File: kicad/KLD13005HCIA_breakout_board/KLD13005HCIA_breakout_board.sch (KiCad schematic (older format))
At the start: 7 parts, among them J1 Pin Headers, J2 Conn_01x24_Male, J3 Capacitive Touch Sensor, Q1 Q_NMOS_GSD

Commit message: Create initial PCB design
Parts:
- J1: footprint (none) -> Connector_PinSocket_2.54mm:PinSocket_1x10_P2.54mm_Vertical
- J2: footprint (none) -> 687124183622:687124183622
- J3: footprint (none) -> BM20B(0.8)-10DS-0.4V(51):BM20B(0.8)-10DS-0.4V(51)
- Q1: footprint (none) -> bss138:BSS138
- R1, R2, R3: footprint (none) -> Resistor_SMD:R_0603_1608Metric
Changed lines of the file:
@@
 F 0 "J1" H 950 2150 50  0000 C CNN
 F 1 "Pin Headers" H 1000 2050 50  0000 C CNN
-F 2 "" H 850 1450 50  0001 C CNN
+F 2 "Connector_PinSocket_2.54mm:PinSocket_1x10_P2.54mm_Vertical" H 850 1450 50  0001 C CNN
 F 3 "~" H 850 1450 50  0001 C CNN
 	1    850  1450
@@
 F 0 "J3" H 4250 1767 50  0000 C CNN
 F 1 "Capacitive Touch Sensor" H 4250 1676 50  0000 C CNN
-F 2 "" H 4200 1350 50  0001 C CNN
+F 2 "BM20B(0.8)-10DS-0.4V(51):BM20B(0.8)-10DS-0.4V(51)" H 4200 1350 50  0001 C CNN
 F 3 "~" H 4200 1350 50  0001 C CNN
 	1    4200 1350
@@
 F 0 "R2" H 4209 2246 50  0000 L CNN
 F 1 "10K" H 4209 2155 50  0000 L CNN
-F 2 "" H 4150 2200 50  0001 C CNN
+F 2 "Resistor_SMD:R_0603_1608Metric" H 4150 2200 50  0001 C CNN
 F 3 "~" H 4150 2200 50  0001 C CNN
 	1    4150 2200
@@
 F 0 "Q1" H 4105 3296 50  0000 L CNN
 F 1 "Q_NMOS_GSD" H 4105 3205 50  0000 L CNN
-F 2 "" H 4100 3350 50  0001 C CNN
+F 2 "bss138:BSS138" H 4100 3350 50  0001 C CNN
 F 3 "~" H 3900 3250 50  0001 C CNN
 	1    3900 3250
@@
 F 0 "R1" H 3859 2896 50  0000 L CNN
 F 1 "10K" H 3859 2805 50  0000 L CNN
-F 2 "" H 3800 2850 50  0001 C CNN
+F 2 "Resistor_SMD:R_0603_1608Metric" H 3800 2850 50  0001 C CNN
 F 3 "~" H 3800 2850 50  0001 C CNN
 	1    3800 2850
@@
 F 0 "R3" H 4259 2896 50  0000 L CNN
 F 1 "2.5K" H 4259 2805 50  0000 L CNN
-F 2 "" H 4200 2850 50  0001 C CNN
+F 2 "Resistor_SMD:R_0603_1608Metric" H 4200 2850 50  0001 C CNN
 F 3 "~" H 4200 2850 50  0001 C CNN
 	1    4200 2850
@@
 F 0 "J2" H 2300 3400 50  0000 C CNN
 F 1 "Conn_01x24_Male" H 2300 3300 50  0000 C CNN
-F 2 "" H 2200 2050 50  0001 C CNN
+F 2 "687124183622:687124183622" H 2200 2050 50  0001 C CNN
 F 3 "~" H 2200 2050 50  0001 C CNN
 	1    2200 2050

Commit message: Update schematic. Move connector position
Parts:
- R1: value 10K -> 10
- R3: value 2.5K -> 2.2K
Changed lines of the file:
@@
 P 3800 2850
 F 0 "R1" H 3859 2896 50  0000 L CNN
-F 1 "10K" H 3859 2805 50  0000 L CNN
+F 1 "10" H 3859 2805 50  0000 L CNN
 F 2 "Resistor_SMD:R_0603_1608Metric" H 3800 2850 50  0001 C CNN
 F 3 "~" H 3800 2850 50  0001 C CNN
@@
 P 4200 2850
 F 0 "R3" H 4259 2896 50  0000 L CNN
-F 1 "2.5K" H 4259 2805 50  0000 L CNN
+F 1 "2.2K" H 4259 2805 50  0000 L CNN
 F 2 "Resistor_SMD:R_0603_1608Metric" H 4200 2850 50  0001 C CNN
 F 3 "~" H 4200 2850 50  0001 C CNN

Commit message: Fix pin arrangement for capacitive touch sensor. Rename D/C pin to SCK
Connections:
- net CAPSENS_INT: now also J1.8 (Pin_8); no longer J1.10 (Pin_10)
- net I2C_SCL: now also J1.10 (Pin_10); no longer J1.8 (Pin_8)
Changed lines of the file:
@@
 Text Label 1050 1550 0    50   ~ 0
 LCD_DC
-Text Label 1050 1950 0    50   ~ 0
+Text Label 1050 1750 0    50   ~ 0
 CAPSENS_INT
 $Comp
@@
 Text Label 1050 1850 0    50   ~ 0
 I2C_SDA
-Text Label 1050 1750 0    50   ~ 0
+Text Label 1050 1950 0    50   ~ 0
 I2C_SCL
 Text Label 1050 1250 0    50   ~ 0

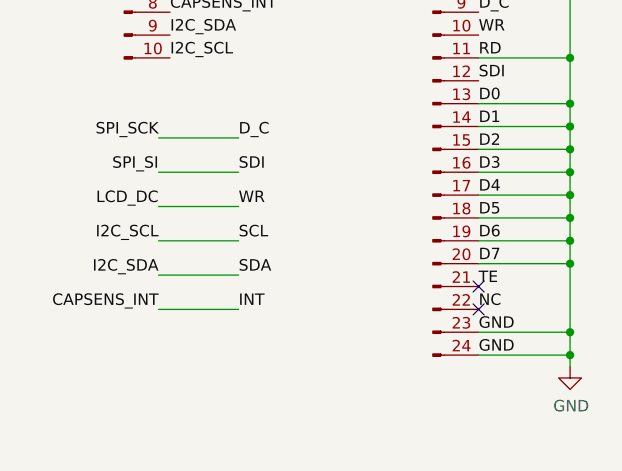
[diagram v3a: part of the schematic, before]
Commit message: Swap INT and SDC pin labels. Add two 10K pull-up resistors for I2C communication
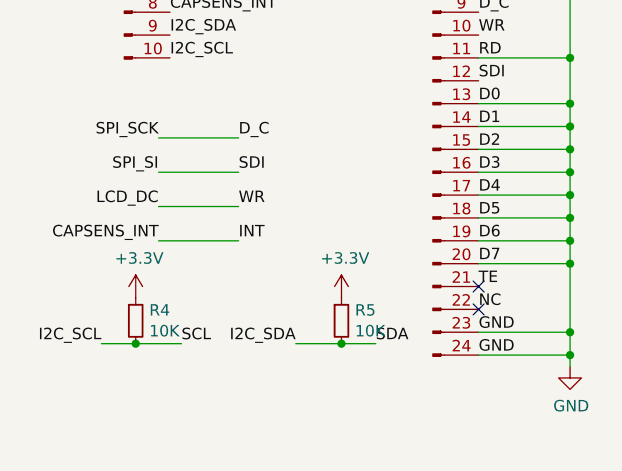
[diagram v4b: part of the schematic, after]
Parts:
- added R4, R5: 10K, Resistor_SMD:R_0603_1608Metric, symbol Device:R_Small
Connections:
- net +3V3: now also R4.1, R5.1
- net I2C_SCL: now also R4.2
- net I2C_SDA: now also R5.2
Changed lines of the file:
@@
 Wire Wire Line
 	1000 2600 1350 2600
+Text Label 1100 3200 0    50   ~ 0
+SCL
+Text Label 1950 3200 0    50   ~ 0
+SDA
 Text Label 1350 2750 0    50   ~ 0
-SCL
-Text Label 1350 2900 0    50   ~ 0
-SDA
-Text Label 1350 3050 0    50   ~ 0
 INT
+Text Label 750  3200 2    50   ~ 0
+I2C_SCL
+Text Label 1600 3200 2    50   ~ 0
+I2C_SDA
 Text Label 1000 2750 2    50   ~ 0
-I2C_SCL
-Text Label 1000 2900 2    50   ~ 0
-I2C_SDA
-Text Label 1000 3050 2    50   ~ 0
 CAPSENS_INT
 Wire Wire Line
+	750  3200 900  3200
+Wire Wire Line
+	1600 3200 1800 3200
+Wire Wire Line
 	1000 2750 1350 2750
-Wire Wire Line
-	1000 2900 1350 2900
-Wire Wire Line
-	1000 3050 1350 3050
 $Comp
 L Connector:Conn_01x24_Male J2
@@
 Wire Wire Line
 	2800 3250 2800 3300
+$Comp
+L Device:R_Small R4
+U 1 1 61C007E4
+P 900 3100
+F 0 "R4" H 959 3146 50  0000 L CNN
+F 1 "10K" H 959 3055 50  0000 L CNN
+F 2 "Resistor_SMD:R_0603_1608Metric" H 900 3100 50  0001 C CNN
+F 3 "~" H 900 3100 50  0001 C CNN
+	1    900  3100
+	1    0    0    -1
+$EndComp
+Connection ~ 900  3200
+Wire Wire Line
+	900  3200 1100 3200
+$Comp
+L Device:R_Small R5
+U 1 1 61C00E6A
+P 1800 3100
+F 0 "R5" H 1859 3146 50  0000 L CNN
+F 1 "10K" H 1859 3055 50  0000 L CNN
+F 2 "Resistor_SMD:R_0603_1608Metric" H 1800 3100 50  0001 C CNN
+F 3 "~" H 1800 3100 50  0001 C CNN
+	1    1800 3100
+	1    0    0    -1
+$EndComp
+Connection ~ 1800 3200
+Wire Wire Line
+	1800 3200 1950 3200
+$Comp
+L power:+3.3V #PWR0101
+U 1 1 61C01D1E
+P 900 3000
+F 0 "#PWR0101" H 900 2850 50  0001 C CNN
+F 1 "+3.3V" H 915 3173 50  0000 C CNN
+F 2 "" H 900 3000 50  0001 C CNN
+F 3 "" H 900 3000 50  0001 C CNN
+	1    900  3000
+	1    0    0    -1
+$EndComp
+$Comp
+L power:+3.3V #PWR0102
+U 1 1 61C0258F
+P 1800 3000
+F 0 "#PWR0102" H 1800 2850 50  0001 C CNN
+F 1 "+3.3V" H 1815 3173 50  0000 C CNN
+F 2 "" H 1800 3000 50  0001 C CNN
+F 3 "" H 1800 3000 50  0001 C CNN
+	1    1800 3000
+	1    0    0    -1
+$EndComp
 $EndSCHEMATC
